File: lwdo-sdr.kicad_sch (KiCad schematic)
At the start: 28 parts, among them J101 IN1, J102 IN2, J103 IN3, J104 IN4, J105 USB_B, J106 CLK_OUT, J107 REF_IN

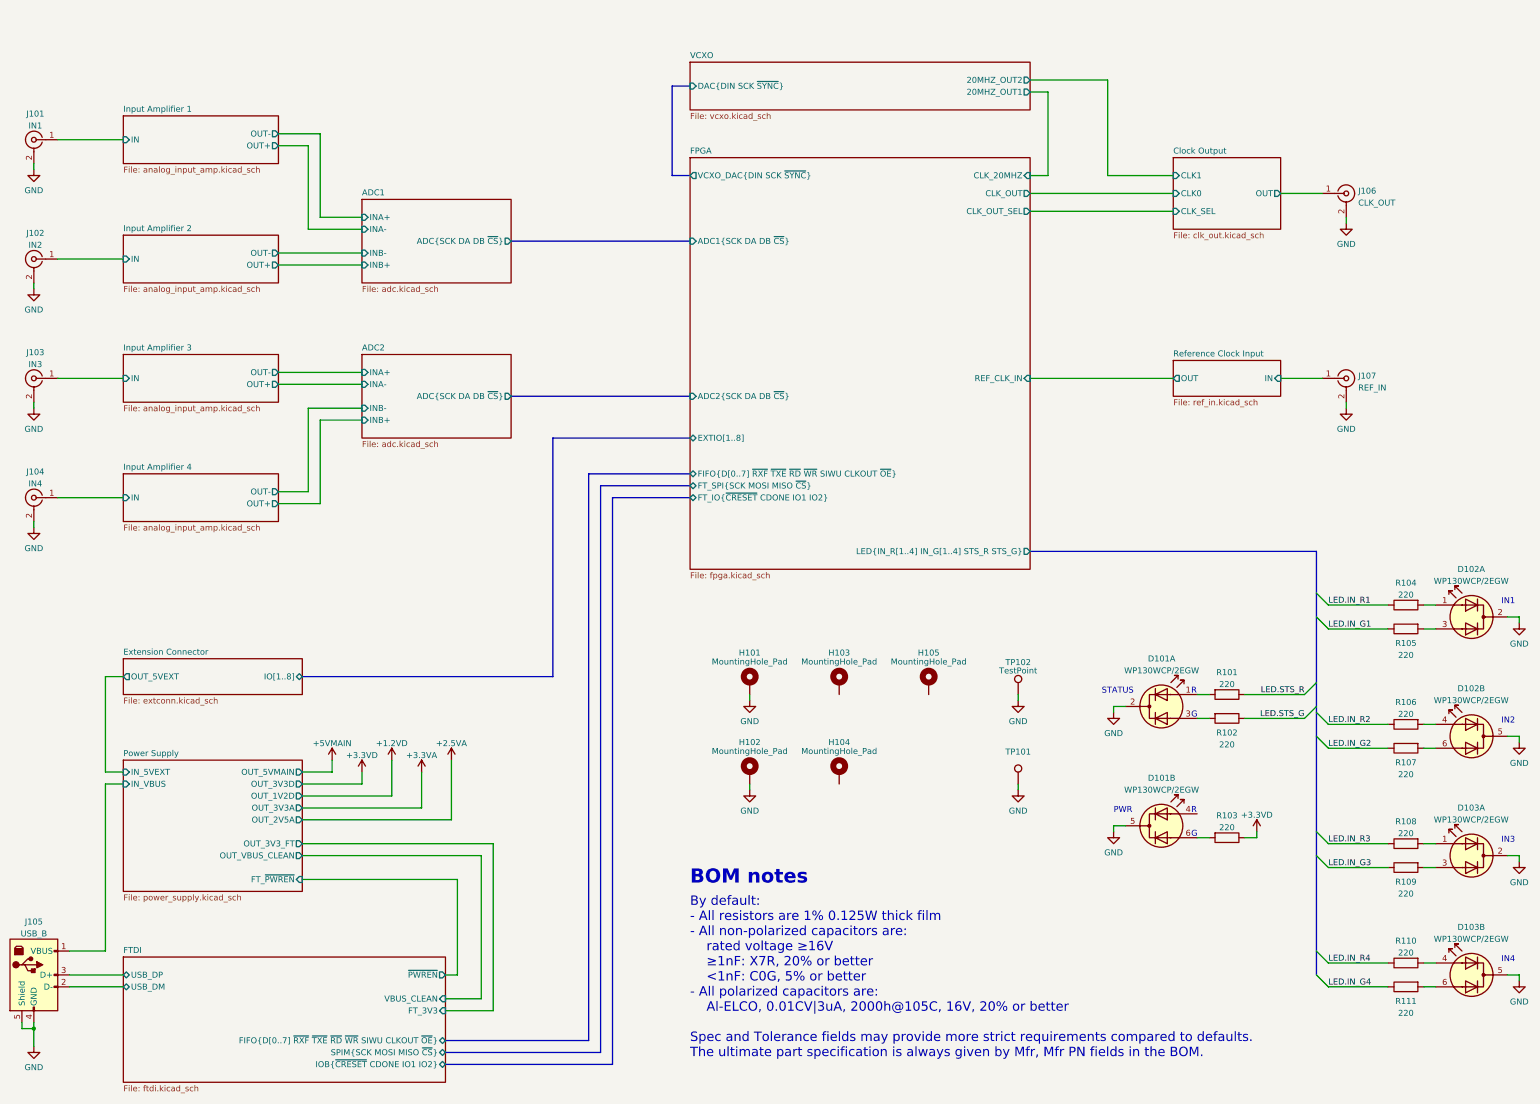
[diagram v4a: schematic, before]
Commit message: Redesign VOCM network, power FDA from 3v3 directly
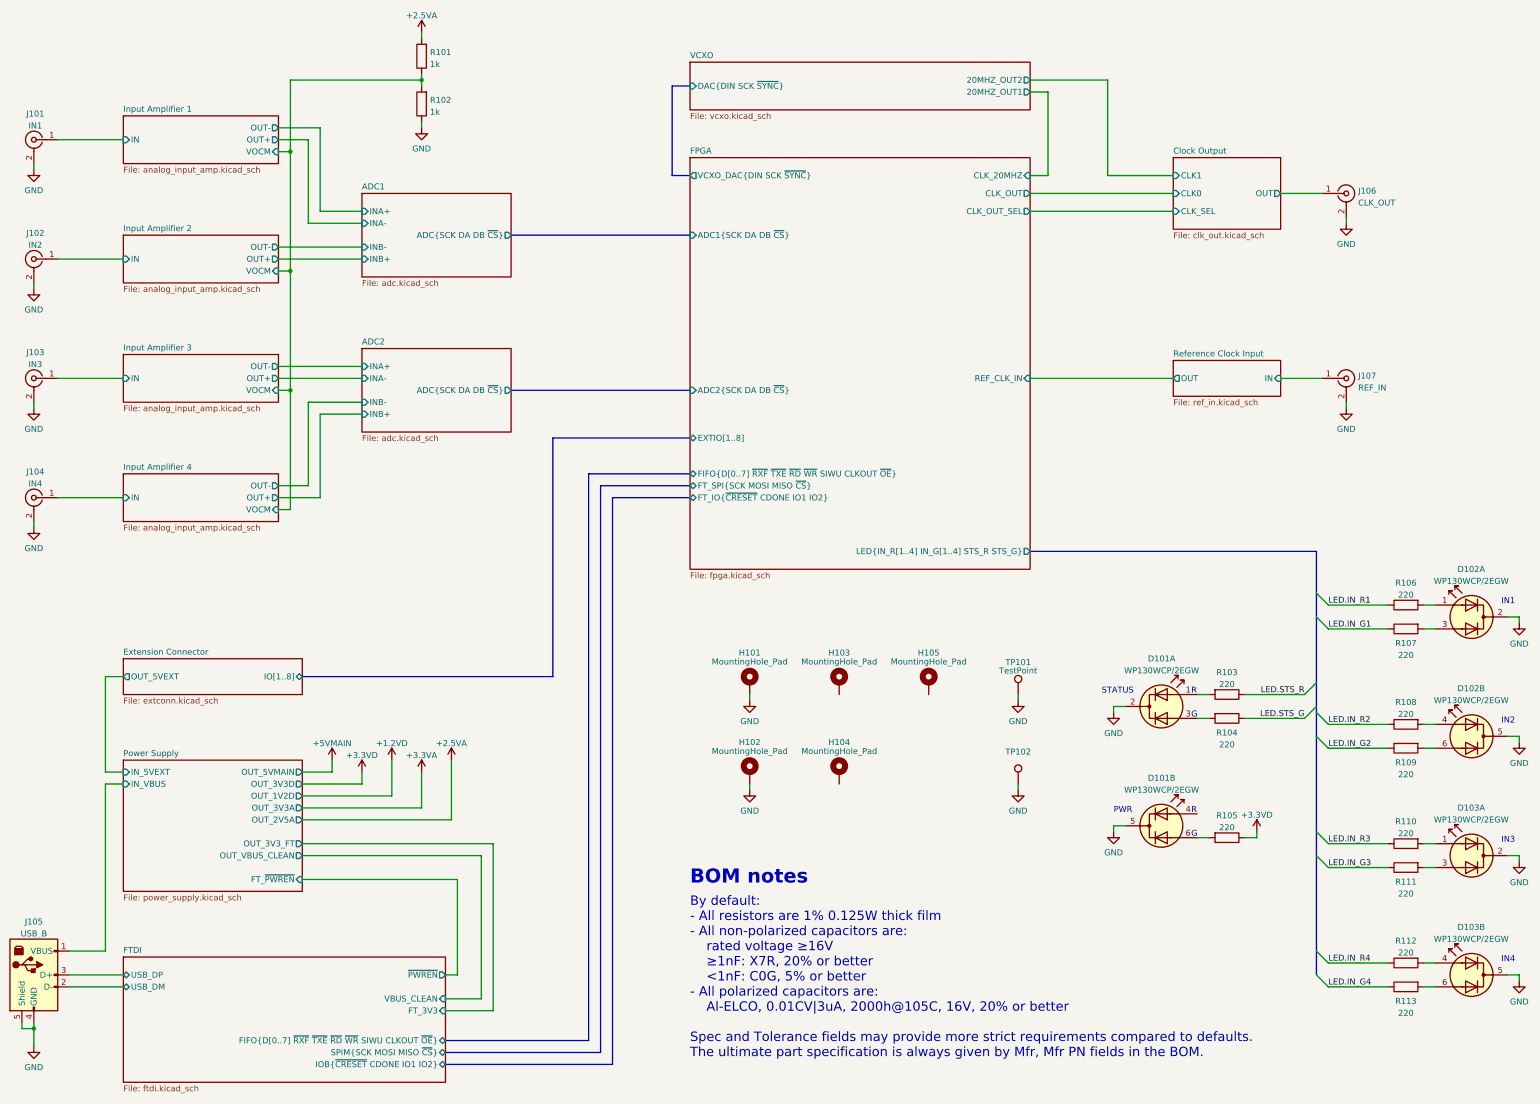
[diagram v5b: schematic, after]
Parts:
- added R101, R102: 1k, Resistor_SMD:R_0805_2012Metric, symbol Device:R
- renumbered R101 to R103, R102 to R104, R103 to R105, R104 to R106, R105 to R107, R106 to R108, R107 to R109, R108 to R110, R109 to R111, R110 to R112, R111 to R113, TP102 to TP101, TP101 to TP102
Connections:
- net +2.5VA: now also R101.2
- net GND: now also R102.1
- new net Input Amplifier 1/VOCM: R101.1, R102.2
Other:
- sheet Input Amplifier 1 ports: added VOCM; removed none
- sheet Input Amplifier 2 ports: added VOCM; removed none
- sheet Input Amplifier 3 ports: added VOCM; removed none
- sheet Input Amplifier 4 ports: added VOCM; removed none

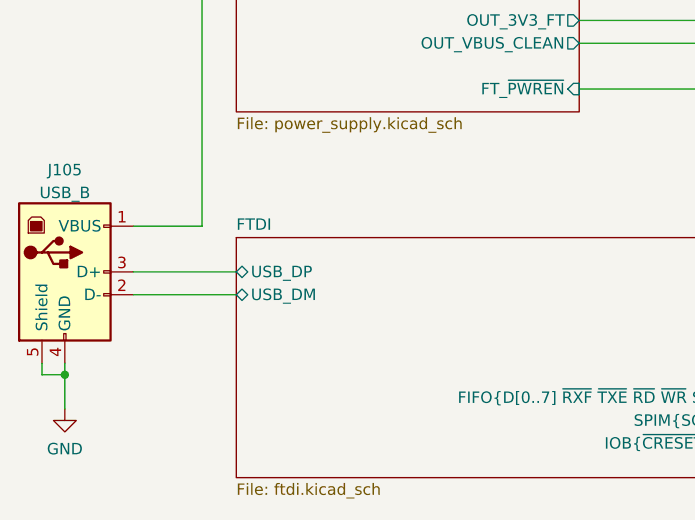
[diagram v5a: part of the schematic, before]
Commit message: Rename USB dp,dm to d+,d- to make pcbnew happy
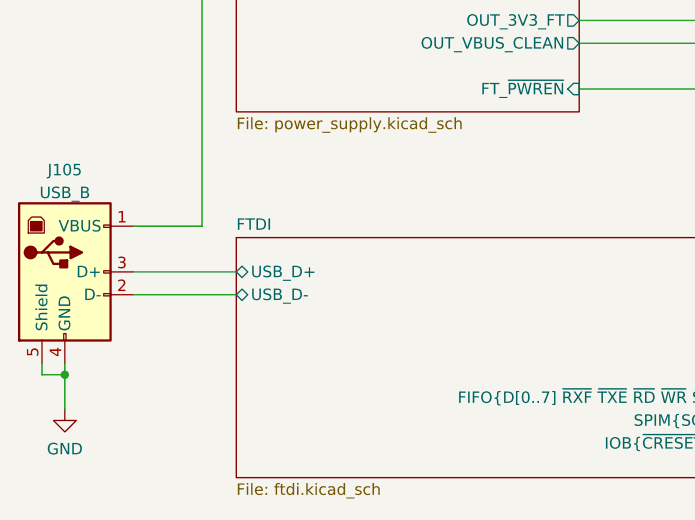
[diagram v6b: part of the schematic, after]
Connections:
- net FTDI/USB_DM renamed FTDI/USB_D-
- net FTDI/USB_DP renamed FTDI/USB_D+
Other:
- sheet FTDI ports: added USB_D+, USB_D-; removed USB_DM, USB_DP
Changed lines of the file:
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@@
       (effects (font (size 1.27 1.27)) (justify left top))
-    )
-    (pin "USB_DP" bidirectional (at 82.55 228.6 180)
-      (effects (font (size 1.27 1.27)) (justify left))
-    )
-    (pin "USB_DM" bidirectional (at 82.55 231.14 180)
-      (effects (font (size 1.27 1.27)) (justify left))
     )
     (pin "~{PWREN}" output (at 151.13 228.6 0)
@@
       (effects (font (size 1.27 1.27)) (justify right))
     )
+    (pin "USB_D-" bidirectional (at 82.55 231.14 180)
+      (effects (font (size 1.27 1.27)) (justify left))
+    )
+    (pin "USB_D+" bidirectional (at 82.55 228.6 180)
+      (effects (font (size 1.27 1.27)) (justify left))
+    )
   )

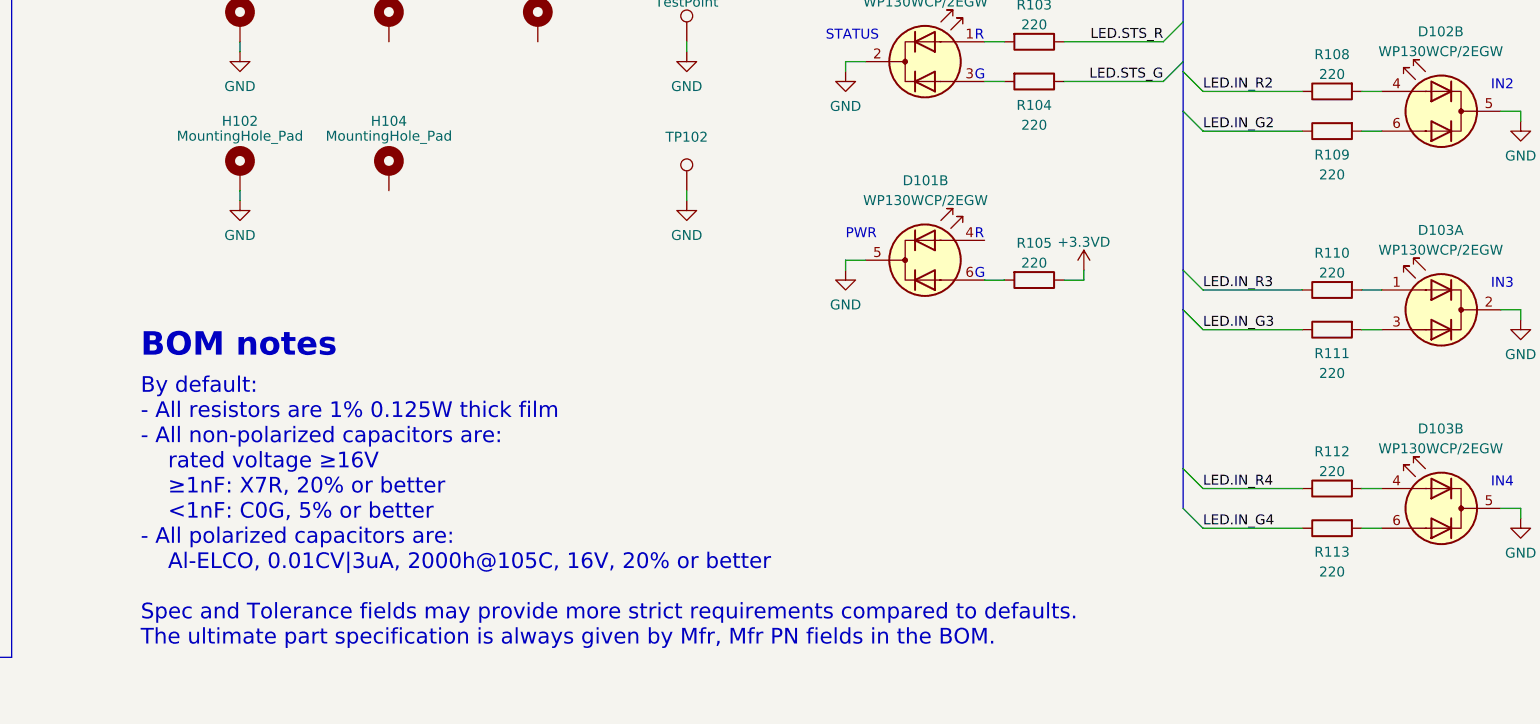
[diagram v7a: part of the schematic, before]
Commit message: Replace 10uf al-elco by tantalum -Space savings (0805 vs 4mm cylinder)
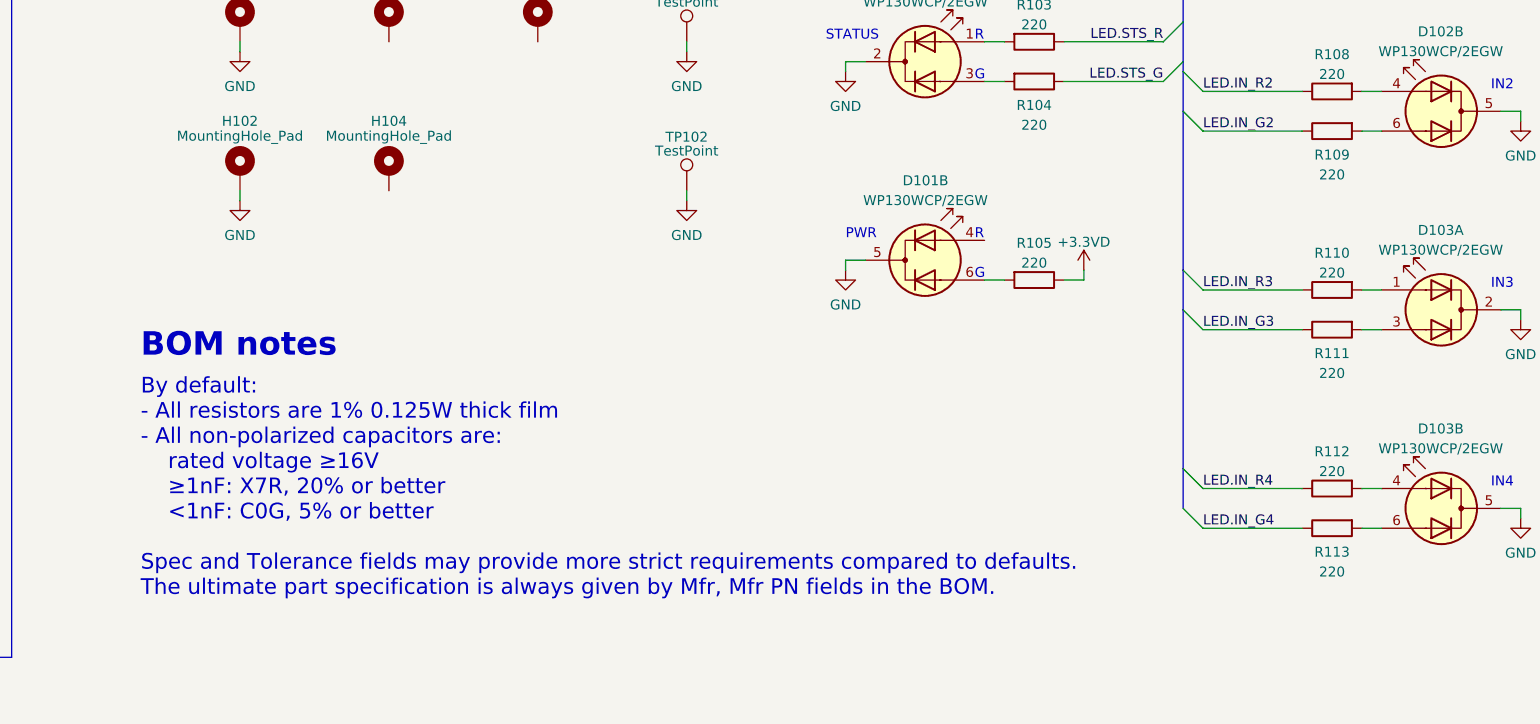
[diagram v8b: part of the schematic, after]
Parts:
- TP102: value (none) -> TestPoint; footprint (none) -> TestPoint:TestPoint_Bridge_Pitch5.08mm_Drill1.3mm
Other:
- note added: "By default: - All resistors are 1% 0.125W thick film - All non-polarized capacitors are: rated voltage ≥16V ≥1nF: X7R, 20% or better <1nF: C0G, 5% or better Spec and Tolerance fields may provide more strict requirements compared to defaults. The ultimate part specification is always given by Mfr, Mfr PN fields in the BOM."
- note removed: "By default: - All resistors are 1% 0.125W thick film - All non-polarized capacitors are: rated voltage ≥16V ≥1nF: X7R, 20% or better <1nF: C0G, 5% or better - All polarized capacitors are: Al-ELCO, 0.01CV|3uA, 2000h@105C, 16V, 20% or better Spec and Tolerance fields may provide more strict requirements compared to defaults. The ultimate part specification is always given by Mfr, Mfr PN fields in 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"
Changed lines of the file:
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@@
     (effects (font (size 1.27 1.27)) (justify left bottom))
   )
-  (text "By default:\n- All resistors are 1% 0.125W thick film\n- All non-polarized capacitors are:\n    rated voltage ≥16V\n    ≥1nF: X7R, 20% or better\n    <1nF: C0G, 5% or better\n- All polarized capacitors are:\n    Al-ELCO, 0.01CV|3uA, 2000h@105C, 16V, 20% or better\n\nSpec and Tolerance fields may provide more strict requirements compared to defaults.\nThe ultimate part specification is always given by Mfr, Mfr PN fields in the BOM.\n"
-    (at 203.2 246.38 0)
+  (text "By default:\n- All resistors are 1% 0.125W thick film\n- All non-polarized capacitors are:\n    rated voltage ≥16V\n    ≥1nF: X7R, 20% or better\n    <1nF: C0G, 5% or better\n\nSpec and Tolerance fields may provide more strict requirements compared to defaults.\nThe ultimate part specification is always given by Mfr, Mfr PN fields in the BOM.\n"
+    (at 203.2 240.03 0)
     (effects (font (size 2 2)) (justify left bottom))
   )
@@
     (in_bom yes) (on_board yes)
     (property "Reference" "TP102" (id 0) (at 273.05 181.102 0))
-    (property "Value" "" (id 1) (at 273.05 182.88 0))
-    (property "Footprint" "" (id 2) (at 278.13 187.96 0)
+    (property "Value" "TestPoint" (id 1) (at 273.05 182.88 0))
+    (property "Footprint" "TestPoint:TestPoint_Bridge_Pitch5.08mm_Drill1.3mm" (id 2) (at 278.13 187.96 0)
       (effects (font (size 1.27 1.27)) hide)
     )
@@
     )
     (path "/d26f84ce-09cf-42fc-96be-2f9ccec4a29a/cf86c9d9-9f53-4ead-bc03-89b12ff4bfcb"
-      (reference "C220") (unit 1) (value "10u") (footprint "Capacitor_SMD:CP_Elec_4x5.8")
+      (reference "C220") (unit 1) (value "10u") (footprint "Capacitor_Tantalum_SMD:CP_EIA-2012-15_AVX-P")
     )
     (path "/d26f84ce-09cf-42fc-96be-2f9ccec4a29a/36960480-e38c-4314-9361-a40581bc7006"
@@
     )
     (path "/d26f84ce-09cf-42fc-96be-2f9ccec4a29a/a45f695a-539d-4af4-a27d-693e87239797"
-      (reference "C222") (unit 1) (value "10u") (footprint "Capacitor_SMD:CP_Elec_4x5.8")
+      (reference "C222") (unit 1) (value "10u") (footprint "Capacitor_Tantalum_SMD:CP_EIA-2012-15_AVX-P")
     )
     (path "/d26f84ce-09cf-42fc-96be-2f9ccec4a29a/28fcda05-4b8a-44c0-8233-d087b0cff761"
@@
     )
     (path "/d9555bc4-8099-43af-87d5-6a781e586fb5/8d79534f-b254-4741-a623-7fd2f620925c"
-      (reference "C701") (unit 1) (value "10u") (footprint "Capacitor_SMD:CP_Elec_4x5.8")
+      (reference "C701") (unit 1) (value "10u") (footprint "Capacitor_Tantalum_SMD:CP_EIA-2012-15_AVX-P")
     )
     (path "/d9555bc4-8099-43af-87d5-6a781e586fb5/0db57b81-8ec8-46a3-a1d4-3f3d6a40ebfe"
-      (reference "C702") (unit 1) (value "10u") (footprint "Capacitor_SMD:CP_Elec_4x5.8")
+      (reference "C702") (unit 1) (value "10u") (footprint "Capacitor_Tantalum_SMD:CP_EIA-2012-15_AVX-P")
     )
     (path "/d9555bc4-8099-43af-87d5-6a781e586fb5/1dba2d6f-8fce-455e-b2e9-16dc1af898fc"
@@
     )
     (path "/9548dea3-b43c-4aa4-a7c3-e0288b5927b1/8d79534f-b254-4741-a623-7fd2f620925c"
-      (reference "C801") (unit 1) (value "10u") (footprint "Capacitor_SMD:CP_Elec_4x5.8")
+      (reference "C801") (unit 1) (value "10u") (footprint "Capacitor_Tantalum_SMD:CP_EIA-2012-15_AVX-P")
     )
     (path "/9548dea3-b43c-4aa4-a7c3-e0288b5927b1/0db57b81-8ec8-46a3-a1d4-3f3d6a40ebfe"
-      (reference "C802") (unit 1) (value "10u") (footprint "Capacitor_SMD:CP_Elec_4x5.8")
+      (reference "C802") (unit 1) (value "10u") (footprint "Capacitor_Tantalum_SMD:CP_EIA-2012-15_AVX-P")
     )
     (path "/9548dea3-b43c-4aa4-a7c3-e0288b5927b1/1dba2d6f-8fce-455e-b2e9-16dc1af898fc"
